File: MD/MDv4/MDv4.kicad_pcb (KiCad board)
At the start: 2 copper layers, 61 x 66 mm, 42 parts, among them J1 XT60PW-M, J2 XT60PW-M, J3 XT30PW-M, J4 XT30PW-M

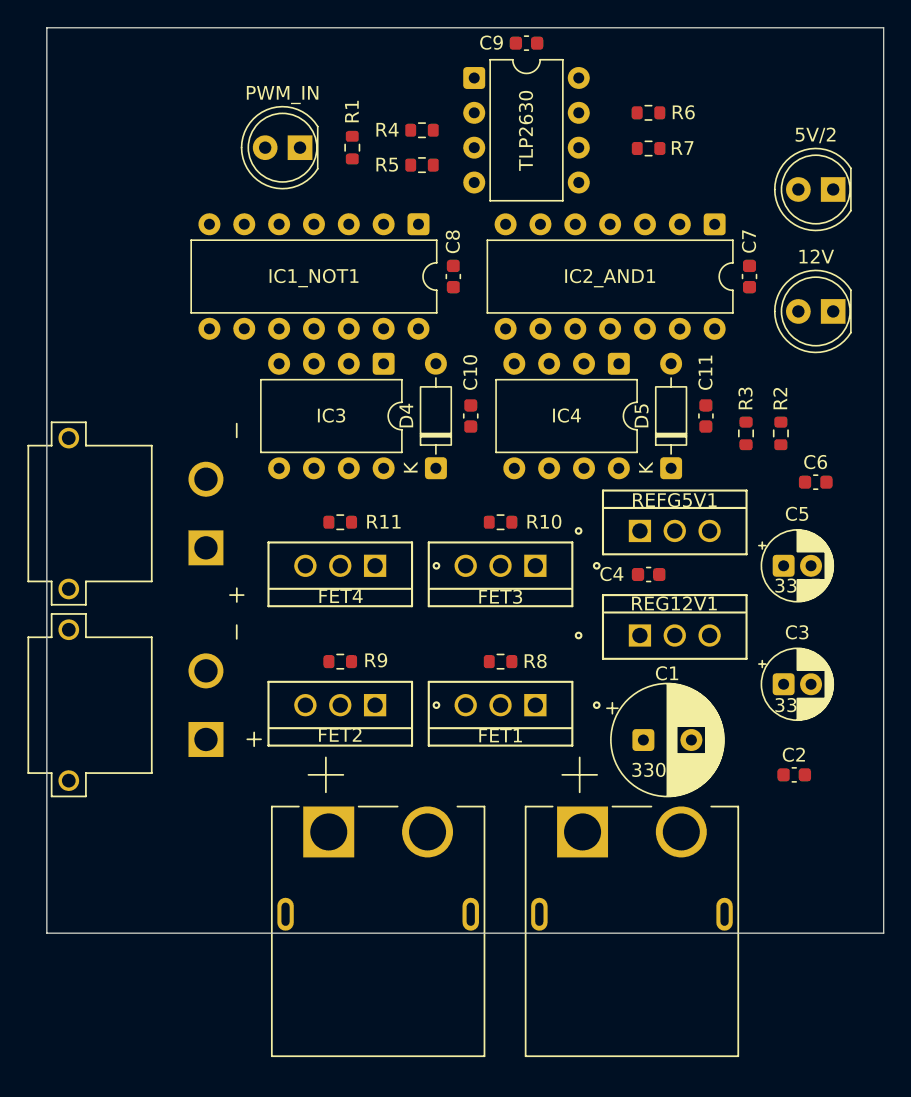
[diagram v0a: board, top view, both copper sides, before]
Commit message: 配線のために配置変え
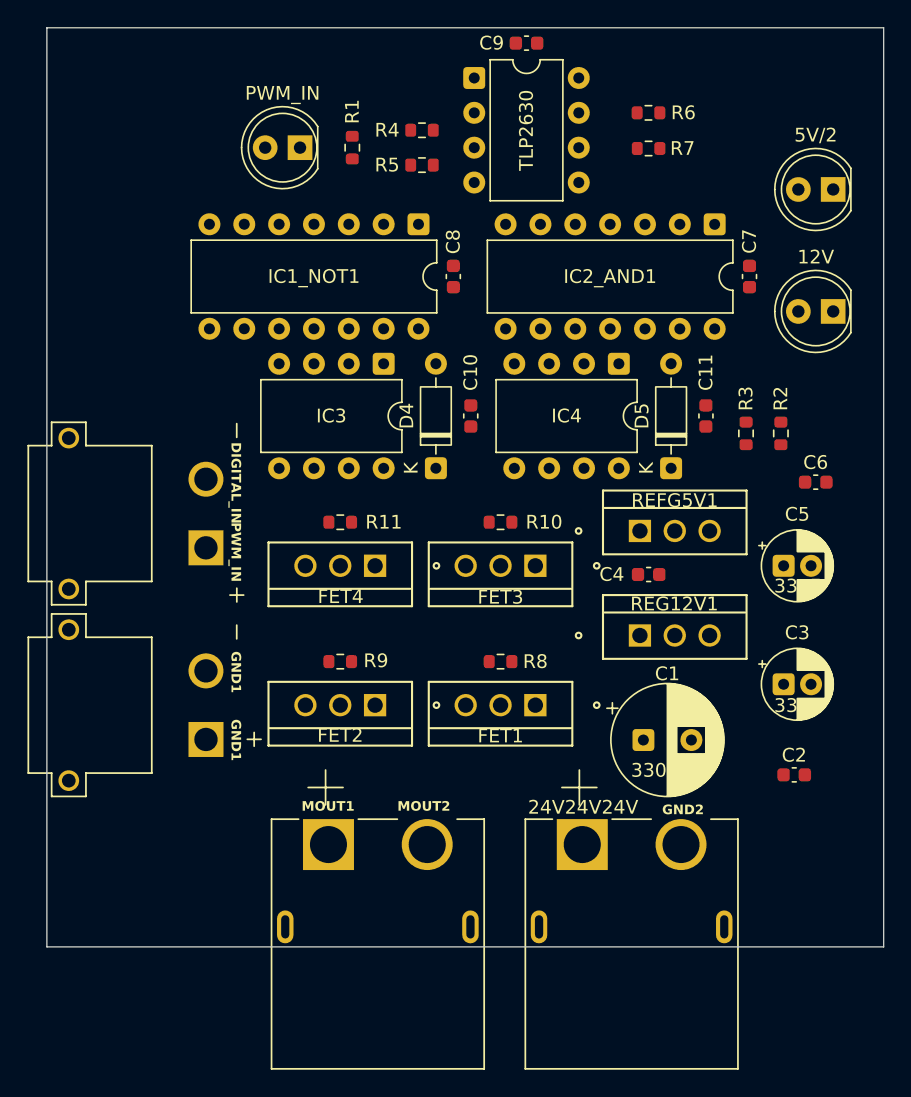
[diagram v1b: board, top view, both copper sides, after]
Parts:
- moved J1 0.92 mm to (79.6, 135.5)
- moved J2 0.92 mm to (98.1, 135.5)
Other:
- board size 61 x 66 mm -> 61 x 67 mm
- board text added: "24V24V24V"
- board text added: "DIGITAL_IN"
- board text added: "GND1"
- board text added: "GND2"
- board text added: "MOUT1"
- board text added: "MOUT2"
- board text added: "PWM_IN"
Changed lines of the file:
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@@
 	(footprint "XT60PW-M:AMASS_XT60PW-M"
 		(layer "F.Cu")
-		(at 98.11 134.62 180)
+		(at 98.088 135.54 180)
 		(property "Reference" "J2"
 			(at -4.8236 -13.51498 0)
@@
 	(footprint "XT60PW-M:AMASS_XT60PW-M"
 		(layer "F.Cu")
-		(at 79.61 134.62 180)
+		(at 79.588 135.54 180)
 		(property "Reference" "J1"
 			(at -4.8236 -13.51498 0)
@@
 	(gr_rect
 		(start 55.46 70)
-		(end 116.46 136)
+		(end 116.46 137)
 		(stroke
 			(width 0.05)
@@
 		(layer "Edge.Cuts")
 	)
+	(gr_text "PWM_IN"
+		(at 68.834 106.045 270)
+		(layer "F.SilkS" knockout)
+		(effects
+			(font
+				(size 0.7 0.7)
+				(thickness 0.12)
+				(bold yes)
+			)
+			(justify left bottom)
+		)
+	)
+	(gr_text "GND1"
+		(at 68.834 115.443 270)
+		(layer "F.SilkS" knockout)
+		(effects
+			(font
+				(size 0.7 0.7)
+				(thickness 0.12)
+				(bold yes)
+			)
+			(justify left bottom)
+		)
+	)
+	(gr_text "MOUT2"
+		(at 81.004 127.158 0)
+		(layer "F.SilkS" knockout)
+		(effects
+			(font
+				(size 0.7 0.7)
+				(thickness 0.12)
+				(bold yes)
+			)
+			(justify left bottom)
+		)
+	)
+	(gr_text "GND2"
+		(at 100.308 127.412 0)
+		(layer "F.SilkS" knockout)
+		(effects
+			(font
+				(size 0.7 0.7)
+				(thickness 0.12)
+				(bold yes)
+			)
+			(justify left bottom)
+		)
+	)
+	(gr_text "DIGITAL_IN"
+		(at 68.834 100.203 270)
+		(layer "F.SilkS" knockout)
+		(effects
+			(font
+				(size 0.7 0.7)
+				(thickness 0.12)
+				(bold yes)
+			)
+			(justify left bottom)
+		)
+	)
+	(gr_text "GND1"
+		(at 68.834 120.396 270)
+		(layer "F.SilkS" knockout)
+		(effects
+			(font
+				(size 0.7 0.7)
+				(thickness 0.12)
+				(bold yes)
+			)
+			(justify left bottom)
+		)
+	)
+	(gr_text "24V24V24V"
+		(at 90.526 127.412 0)
+		(layer "F.SilkS" knockout)
+		(effects
+			(font
+				(size 1 1)
+				(thickness 0.15)
+			)
+			(justify left bottom)
+		)
+	)
+	(gr_text "MOUT1"
+		(at 74.019 127.158 0)
+		(layer "F.SilkS" knockout)
+		(effects
+			(font
+				(size 0.7 0.7)
+				(thickness 0.12)
+				(bold yes)
+			)
+			(justify left bottom)
+		)
+	)
 	(embedded_fonts no)

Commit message: やばい
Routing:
- net +5V/2: track 0.00 -> 40.2 mm
- net GND1: track 0.00 -> 11.1 mm, vias 0 -> 1
- added copper zone on F.Cu, net +24V
- added copper zone on B.Cu, net GND2
- added copper zone on F.Cu, net GND2
- added copper zone on B.Cu, net MOUT1
- added copper zone on B.Cu, net MOUT2
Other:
- board size 61 x 67 mm -> 61 x 68 mm

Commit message: 一旦表面実装の部品探しの旅に出ます
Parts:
- added REF1**: MountingHole_3.2mm_M3, MountingHole:MountingHole_3.2mm_M3, F.Cu at (60.0, 73.0)
- added REF2**: MountingHole_3.2mm_M3, MountingHole:MountingHole_3.2mm_M3, F.Cu at (112.0, 73.0)
- added REF3**: MountingHole_3.2mm_M3, MountingHole:MountingHole_3.2mm_M3, F.Cu at (112.0, 134.0)
- added REF4**: MountingHole_3.2mm_M3, MountingHole:MountingHole_3.2mm_M3, F.Cu at (60.0, 134.0)
- moved R6 5.34 mm to (94.0, 76.2)
- moved R7 5.34 mm to (94.0, 78.8)
- moved D1 5.33 mm to (68.6, 78.7)
- moved R1 5.33 mm to (72.4, 78.7)
- moved R4 5.33 mm to (77.5, 77.5)
- moved R5 5.33 mm to (77.5, 80.0)
- moved TLP2630 5.33 mm to (81.3, 73.7)
- moved C9 4.96 mm to (85.5, 71.4)
- moved C8 3.82 mm to (81.3, 88.4)
- moved C7 3.81 mm to (102.9, 88.1)
- moved IC1_NOT1 3.81 mm to (78.7, 84.3)
- moved IC2_AND1 3.81 mm to (100.3, 84.3)
- moved R2 1.02 mm to (110.0, 99.6)
- moved D3 0.25 mm to (112.5, 90.7)
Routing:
- net +5V/2: track 40.2 -> 0.00 mm
- net GND1: track 11.1 -> 0.00 mm, vias 1 -> 0
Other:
- board size 61 x 68 mm -> 61 x 69 mm

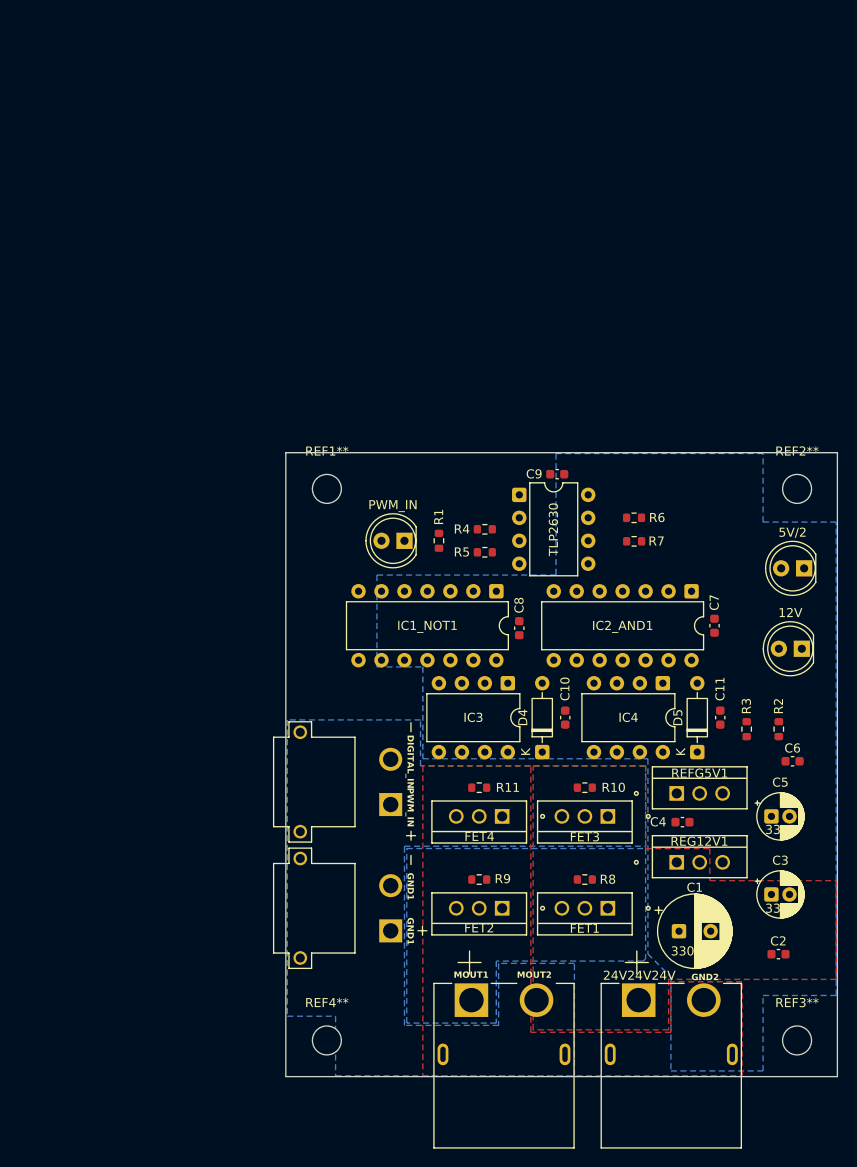
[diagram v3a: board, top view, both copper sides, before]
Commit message: メイン基板変更進捗
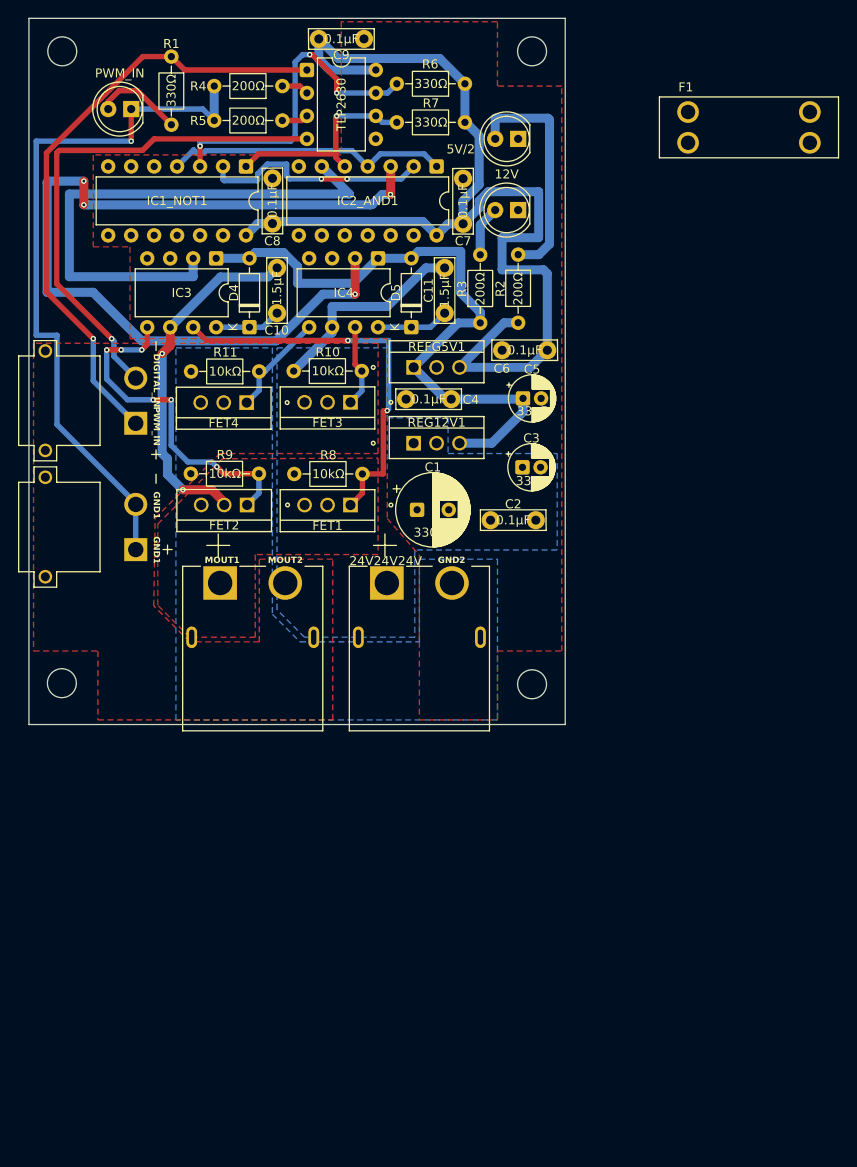
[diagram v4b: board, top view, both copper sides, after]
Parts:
- removed REF1**, REF2**, REF3**, REF4**: MountingHole_3.2mm_M3, MountingHole:MountingHole_3.2mm_M3
- added F1: Fuse, Library:FUSE_3557-15, F.Cu at (106.7, 33.0)
- added REF**: MountingHole_3.2mm_M3, MountingHole:MountingHole_3.2mm_M3, F.Cu at (30.7, 94.5)
- added REF**: MountingHole_3.2mm_M3, MountingHole:MountingHole_3.2mm_M3, F.Cu at (30.7, 24.6)
- added REF**: MountingHole_3.2mm_M3, MountingHole:MountingHole_3.2mm_M3, F.Cu at (82.7, 94.6)
- added REF**: MountingHole_3.2mm_M3, MountingHole:MountingHole_3.2mm_M3, F.Cu at (82.7, 24.6)
- C10, C11, C2, C4, C6, C7, C8, C9: footprint Capacitor_SMD:C_0603_1608Metric -> Library:C_Disc_D11.0mm_W5.0mm_P5.0mm_kai
- J1, J2: footprint XT60PW-M:AMASS_XT60PW-M -> XT60-M:AMASS_XT60PW-M
- R1, R10, R11, R2, R3, R4, R5, R6, R7, R8, R9: footprint Resistor_SMD:R_0603_1608Metric -> Library:R_Axial_DIN0207_L6.3mm_D2.5mm_P10.16mm_Horizontal_kai
- moved R1 61.1 mm to (42.8, 25.2)
- moved D3 57.8 mm to (81.2, 42.2)
- moved C2 57.6 mm to (78.1, 76.4)
- moved D4 57.1 mm to (51.4, 55.1)
- moved D2 57.1 mm to (81.2, 34.3)
- moved IC3 57.0 mm to (47.8, 47.5)
- moved D5 56.6 mm to (69.3, 55.1)
- moved IC4 56.6 mm to (65.7, 47.5)
- moved D1 56.5 mm to (38.4, 31.0)
- moved C6 55.7 mm to (79.4, 57.6)
- moved REFG5V1 55.4 mm to (69.6, 59.6)
- moved C10 54.9 mm to (54.4, 53.6)
- moved C1 54.9 mm to (70.0, 75.3)
- moved IC2_AND1 54.8 mm to (72.1, 37.3)
- moved REG12V1 54.7 mm to (69.6, 67.9)
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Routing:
- net +5V/2: track 0.00 -> 126.3 mm
- net GATE2: track 0.00 -> 99.0 mm, vias 0 -> 4
- net GND1: track 0.00 -> 78.7 mm, vias 0 -> 1
- net +12V: track 0.00 -> 73.1 mm
- net PWM_IN: track 0.00 -> 67.8 mm, vias 0 -> 1
- net GATE1: track 0.00 -> 62.0 mm
- net DIGITAL_IN: track 0.00 -> 56.9 mm, vias 0 -> 1
- net Net-(FET1-G): track 0.00 -> 43.7 mm, vias 0 -> 2
- net MOUT1: track 0.00 -> 39.3 mm, vias 0 -> 2
- net Net-(FET2-G): track 0.00 -> 38.0 mm, vias 0 -> 6
- net PWM_NOT: track 0.00 -> 36.8 mm, vias 0 -> 3
- net PWM1: track 0.00 -> 31.6 mm
- net Net-(D2-A): track 0.00 -> 26.1 mm
- net DIGITAL: track 0.00 -> 25.7 mm, vias 0 -> 2
- net DIGITAL_NOT: track 0.00 -> 24.3 mm, vias 0 -> 1
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- added copper zone on B.Cu, net +24V
- added copper zone on F.Cu, net MOUT1
- added copper zone on F.Cu, net MOUT2
- removed copper zone on F.Cu, net +24V
- removed copper zone on B.Cu, net MOUT1
- removed copper zone on B.Cu, net MOUT2
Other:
- board size 61 x 69 mm -> 59.3 x 78.1 mm
